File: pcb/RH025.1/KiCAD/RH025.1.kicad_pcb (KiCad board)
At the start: 2 copper layers, 65 x 30 mm, 32 parts, among them IC1 FE1.1S, J1 POWER_JACKCOMBO

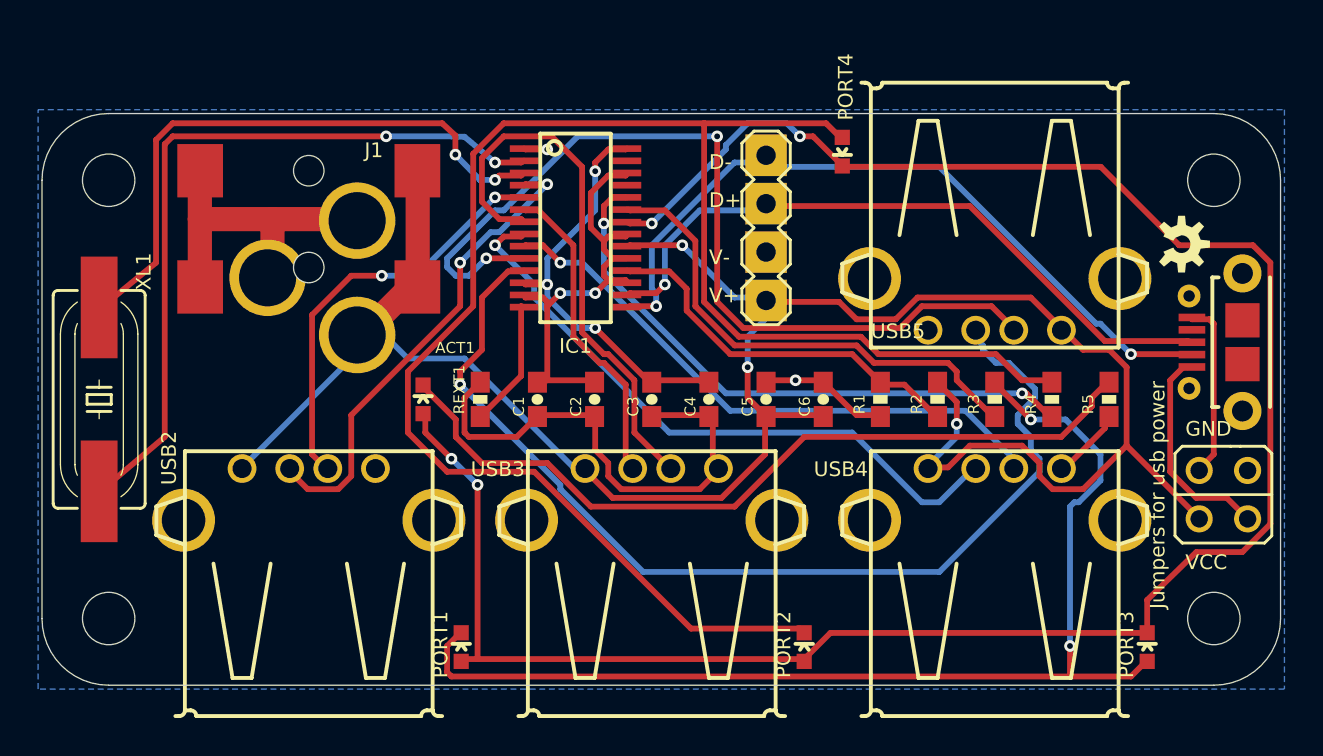
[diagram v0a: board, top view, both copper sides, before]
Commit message: Actually Add KiCAD6 imported project _(was KiCAD 5)_
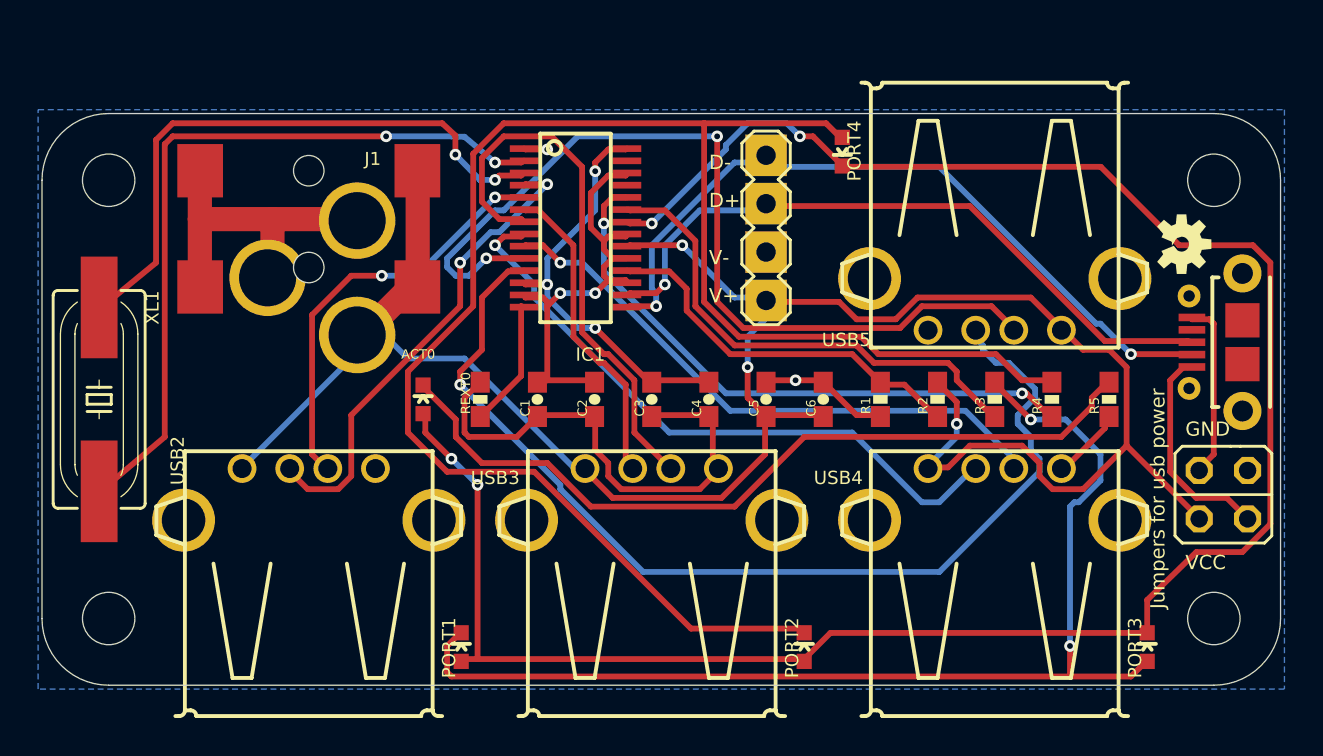
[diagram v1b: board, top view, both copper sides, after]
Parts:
- removed ACT1: LED0603, RH025.1:LED-0603
- removed REXT1: 2.7K, RH025.1:RES-0603
- added ACT0: , RH025.1:LED-0603, F.Cu at (136.0, 105.0)
- added REXT0: 2.7K, RH025.1:RES-0603, F.Cu at (139.0, 105.0)
- JP1: value JP2QE -> (none)
- PORT1, PORT2, PORT3, PORT4: value LED0603 -> (none)
- SV1: value MA04-1 -> (none)
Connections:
- net +3V3 renamed 3V3
- net /D+ renamed D+
- net /D- renamed D-
- J1 pad GND: GND -> (no net)
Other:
- net class Default removed
- board text removed: "Based on design by @MakerBro, https://acrobotic.com This work is licensed under the Creative Commons Attribution-ShareAlike 4.0 International License. To view a copy of this license, visit http://creativecommons.org/licenses/by-sa/4.0/ @richardhawthorn deluxecapacitor.com"
